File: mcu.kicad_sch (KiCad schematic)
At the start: 0 parts

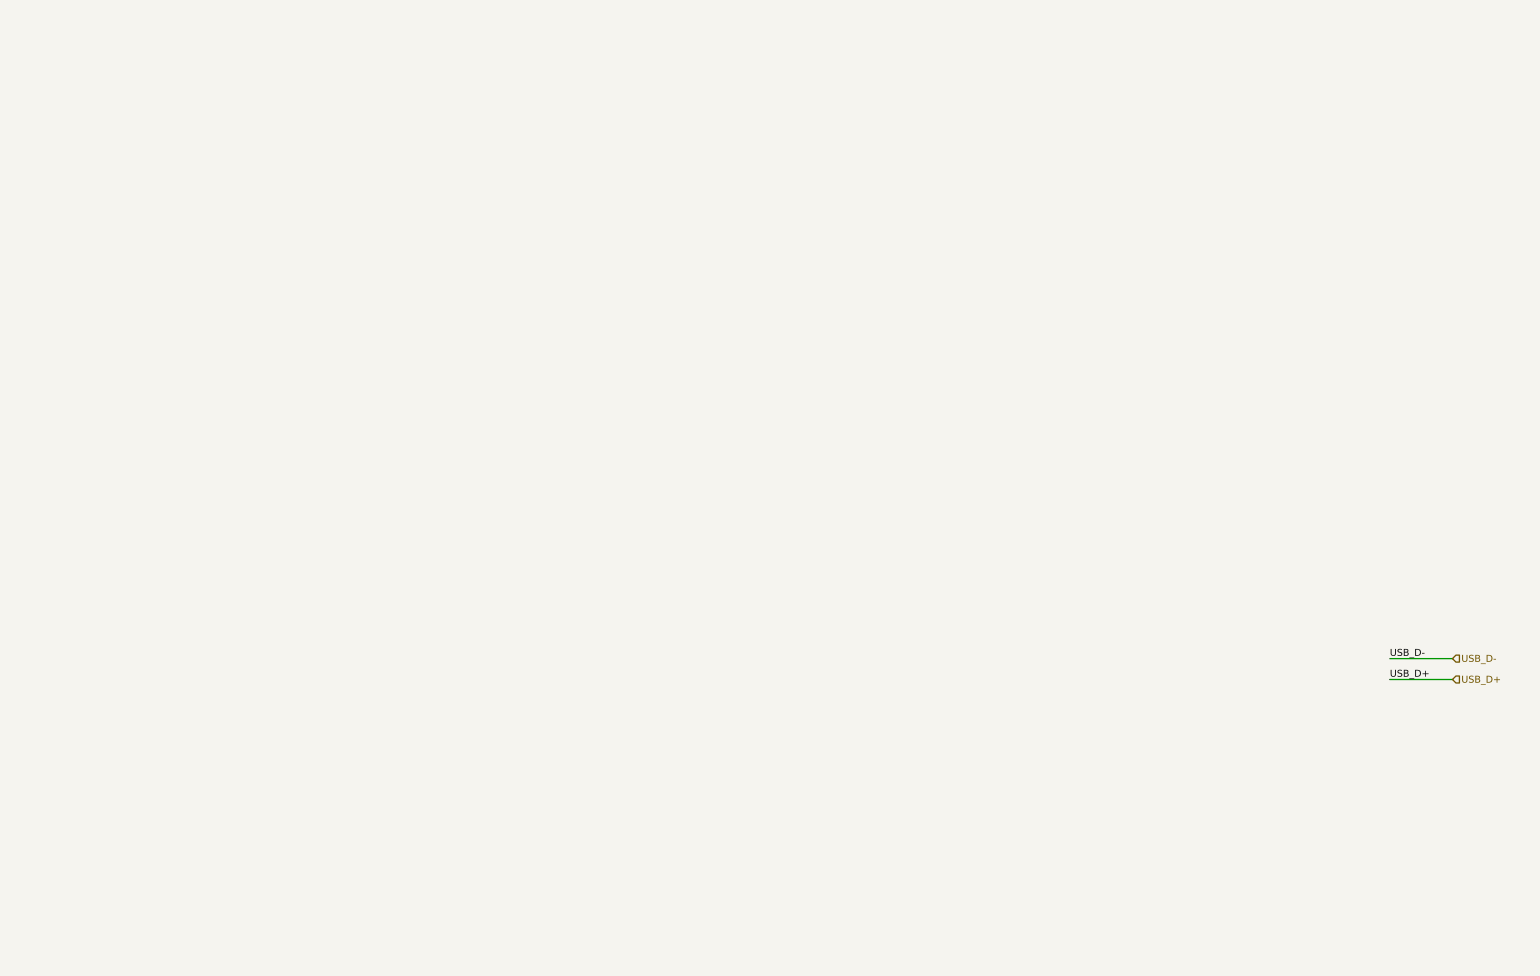
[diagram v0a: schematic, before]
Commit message: Add ESP32-S3-WROOM-1, 5V rail and UI sheet
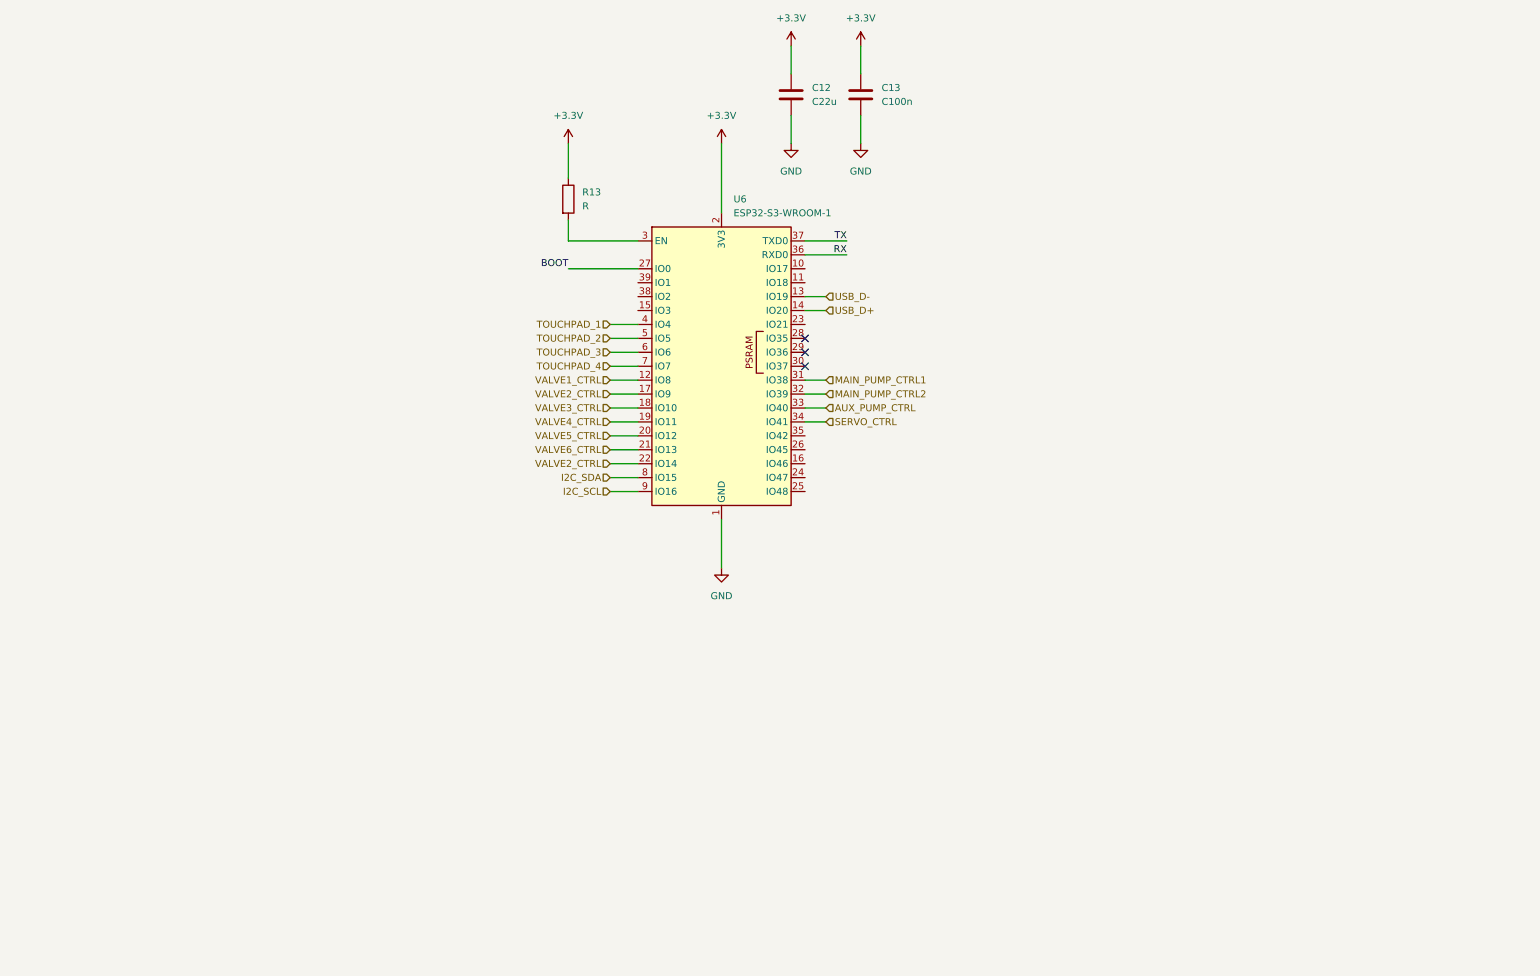
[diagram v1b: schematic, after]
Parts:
- added C12: C22u, symbol Device:C
- added C13: C100n, symbol Device:C
- added R13: R, symbol Device:R
- added U6: ESP32-S3-WROOM-1, RF_Module:ESP32-S3-WROOM-1, symbol RF_Module:ESP32-S3-WROOM-1
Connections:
- net USB_D+: now also U6.14 (IO20)
- net USB_D-: now also U6.13 (IO19)
- new net: R13.2, U6.3 (EN)
- new net +3.3V: C12.1, C13.1, R13.1, U6.2 (3V3)
- new net AUX_PUMP_CTRL: U6.33 (IO40)
- new net BOOT: U6.27 (IO0)
- new net GND: C12.2, C13.2, U6.1 (GND), U6.40 (GND), U6.41 (GND)
- new net I2C_SCL: U6.9 (IO16)
- new net I2C_SDA: U6.8 (IO15)
- new net MAIN_PUMP_CTRL1: U6.31 (IO38)
- new net MAIN_PUMP_CTRL2: U6.32 (IO39)
- new net RX: U6.36 (RXD0)
- new net SERVO_CTRL: U6.34 (IO41)
- new net TOUCHPAD_1: U6.4 (IO4)
- new net TOUCHPAD_2: U6.5 (IO5)
- new net TOUCHPAD_3: U6.6 (IO6)
- new net TOUCHPAD_4: U6.7 (IO7)
- new net TX: U6.37 (TXD0)
- new net VALVE1_CTRL: U6.12 (IO8)
- new net VALVE2_CTRL: U6.17 (IO9), U6.22 (IO14)
- new net VALVE3_CTRL: U6.18 (IO10)
- new net VALVE4_CTRL: U6.19 (IO11)
- new net VALVE5_CTRL: U6.20 (IO12)
- new net VALVE6_CTRL: U6.21 (IO13)
- no-connect marks 0 -> 3

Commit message: Finish first design
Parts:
- added C14: C22u, Capacitor_SMD:C_0805_2012Metric, symbol Device:C
- added JP2: SolderJumper_2_Bridged, Jumper:SolderJumper-2_P1.3mm_Bridged_RoundedPad1.0x1.5mm, symbol Jumper:SolderJumper_2_Bridged
- added R12, R15, R38: R4k7, Resistor_SMD:R_0805_2012Metric, symbol Device:R
- added TP10, TP11, TP12, TP13, TP14, TP16, TP17, TP5, TP6, TP7, TP8, TP9: TestPoint_Small, TestPoint:TestPoint_Pad_D1.5mm, symbol Connector:TestPoint_Small
- added U7: Pico, RPi_Pico:RPi_Pico_SMD_TH, symbol project:Pico
- C12: footprint (none) -> Capacitor_SMD:C_0805_2012Metric; Mouser Part Number (none) -> 187-CL21A226MQQNNNF
- C13: footprint (none) -> Capacitor_SMD:C_0603_1608Metric; Mouser Part Number (none) -> 80-C0603C104K3R7867
- R13: value R -> R100k; footprint (none) -> Resistor_SMD:R_0805_2012Metric; Mouser Part Number (none) -> 660-RK73B2ATTD104J
- U6: Mouser Part Number (none) -> 356-ESP32-S3WROOM1N4
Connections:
- net I2C_SDA is gone; now on net MAIN_PUMP_CTRL2: U6.8 (IO15)
- net TOUCHPAD_2 is gone; now on net AUX_PUMP_CTRL: U6.5 (IO5)
- net TOUCHPAD_4 is gone; now on net MAIN_PUMP_CTRL1: U6.7 (IO7)
- net +3.3V: now also C14.1, R12.1, R15.1, R38.1
- net AUX_PUMP_CTRL: no longer U6.33 (IO40)
- net BOOT: now also TP6.1
- net GND: now also C14.2, U7.43 (GND)
- net MAIN_PUMP_CTRL1: no longer U6.31 (IO38)
- net MAIN_PUMP_CTRL2: no longer U6.32 (IO39)
- net RX: now also TP16.1
- net SERVO_CTRL: now also U6.33 (IO40), TP10.1; no longer U6.34 (IO41)
- net TX: now also TP17.1
- net USB_D+: now also U7.41 (USB_D+)
- net USB_D-: now also U7.42 (USB_D-)
- net VALVE1_CTRL: now also U6.21 (IO13); no longer U6.12 (IO8)
- net VALVE2_CTRL: now also U6.20 (IO12); no longer U6.17 (IO9), U6.22 (IO14)
- net VALVE3_CTRL: now also U6.19 (IO11); no longer U6.18 (IO10)
- net VALVE4_CTRL: now also U6.18 (IO10); no longer U6.19 (IO11)
- net VALVE5_CTRL: now also U6.17 (IO9); no longer U6.20 (IO12)
- net VALVE6_CTRL: now also U6.16 (IO46); no longer U6.21 (IO13)
- net VALVE7_CTRL: now reaches U6.15 (IO3)
- net OLED_SDA: now reaches U6.23 (IO21)
- net OLED_SDA: now also R12.2, TP8.1
- net BUTTON_3: now reaches U6.26 (IO45)
- net ESP32_ENABLE: now reaches R13.2, U6.3 (EN)
- net ESP32_ENABLE: now also TP5.1
- net HX711_CLK: now reaches U6.35 (IO42)
- net HX711_CLK: now also TP11.1
- net BUZZER: now reaches U6.38 (IO2)
- net BUZZER: now also TP13.1
- net 1WIRE_TEMP: now reaches U6.39 (IO1)
- net 1WIRE_TEMP: now also R38.2, TP14.1
- net I2C_SCL: no longer names the net of U6.9 (IO16)
- net TOUCHPAD_1 renamed PWR_FAULT
- net PWR_FAULT: now also TP9.1
- net TOUCHPAD_3 renamed WATER_LEVEL_SENSOR_PIN
- net WATER_LEVEL_SENSOR_PIN: now also JP2.1 (A)
- new net: U7.13 (GND), U7.18 (GND), U7.3 (GND), U7.8 (GND)
- new net: U7.23 (GND), U7.28 (GND), U7.38 (GND)
- new net BUTTON_1: U6.32 (IO39)
- new net BUTTON_2: U6.31 (IO38)
- new net HX711_DAT: TP12.1, U6.34 (IO41)
- new net OLED_SCL: R15.2, TP7.1, U6.22 (IO14)
- new net WATER_LEVEL_SENSOR: JP2.2 (B)
- no-connect marks 3 -> 10
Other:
- note added: "<- Alternatives ->"
- note added: "Check: TODO (boot pin states, alternate funcs)"
- note added: "Don't use PSRAM pins"
- note added: "Don't use pins"
- note added: "ESP32-S3"
- note added: "I2C Pull-Ups"
- note added: "Module cost for ESP32-S3-WROOM-1-XXX: ~3-4 Euro"
- note added: "Module cost for Pico / Pico W: 4~7 Euro"
- note added: "RPI-PICO-W"
- title: (none) -> openautolab - Mainboard
- moved on the sheet: C12, C13, R13, U6

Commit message: Add screen FPC to schematic and remove old OLED stuff
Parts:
- removed C14: C22u, Capacitor_SMD:C_0805_2012Metric, symbol Device:C
- removed JP2: SolderJumper_2_Bridged, Jumper:SolderJumper-2_P1.3mm_Bridged_RoundedPad1.0x1.5mm, symbol Jumper:SolderJumper_2_Bridged
- removed U7: Pico, RPi_Pico:RPi_Pico_SMD_TH, symbol project:Pico
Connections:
- net BUTTON_1: no longer names the net of U6.32 (IO39)
- net BUTTON_2: no longer names the net of U6.31 (IO38)
- net BUTTON_3: no longer names the net of U6.26 (IO45)
- net OLED_SCL: no longer names the net of TP7.1, U6.22 (IO14)
- net OLED_SCL: no longer R15.2
- net OLED_SDA: no longer names the net of TP8.1, U6.23 (IO21)
- net OLED_SDA: no longer R12.2
- net WATER_LEVEL_SENSOR_PIN renamed FLOW_SENSOR
- new net LCD_TOUCH_SCL: R15.2
- new net LCD_TOUCH_SDA: R12.2
- no-connect marks 10 -> 5
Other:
- note removed: "Module cost for Pico / Pico W: 4~7 Euro"
- note removed: "RPI-PICO-W"

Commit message: Fix LCD connector pin mapping and map them to MCU pins
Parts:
- added TP1, TP15, TP2, TP23, TP24, TP27, TP3, TP4: TestPoint_Small, TestPoint:TestPoint_Pad_D1.5mm, symbol Connector:TestPoint_Small
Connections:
- net FLOW_SENSOR: now also TP2.1
- net LCD_MISO: now also U6.11 (IO18), TP15.1
- net LCD_MOSI: now also U6.10 (IO17), TP4.1
- net LCD_RESET: now also U6.9 (IO16), TP1.1
- net LCD_RS: now also U6.12 (IO8), TP3.1
- net LCD_SCK: now also TP7.1, U6.22 (IO14)
- net LCD_TOUCH_INT: now also U6.26 (IO45), TP23.1
- net LCD_TOUCH_RESET: now also TP8.1, U6.23 (IO21)
- net LCD_TOUCH_SCL: now also U6.32 (IO39), TP24.1
- net LCD_TOUCH_SDA: now also U6.31 (IO38), TP27.1

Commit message: Finalize pin mapping, cleanup and layout
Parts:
- removed TP1, TP10, TP11, TP12, TP13, TP14, TP15, TP2, TP23, TP24, TP27, TP3, TP4, TP7, TP8, TP9: TestPoint_Small, TestPoint:TestPoint_Pad_D1.5mm, symbol Connector:TestPoint_Small
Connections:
- net 1WIRE_TEMP: now also U6.9 (IO16); no longer U6.39 (IO1)
- net AUX_PUMP_CTRL: now also U6.12 (IO8); no longer U6.5 (IO5)
- net BUZZER: now also U6.5 (IO5); no longer U6.38 (IO2)
- net FLOW_SENSOR: now also U6.8 (IO15); no longer U6.6 (IO6)
- net HX711_CLK: now also U6.6 (IO6); no longer U6.35 (IO42)
- net HX711_DAT: now also U6.7 (IO7); no longer U6.34 (IO41)
- net LCD_MISO: now also U6.33 (IO40); no longer U6.11 (IO18)
- net LCD_MOSI: now also U6.31 (IO38); no longer U6.10 (IO17)
- net LCD_RESET: now also U6.23 (IO21); no longer U6.9 (IO16)
- net LCD_RS: now also U6.26 (IO45); no longer U6.12 (IO8)
- net LCD_SCK: now also U6.32 (IO39); no longer U6.22 (IO14)
- net LCD_TOUCH_INT: now also U6.34 (IO41); no longer U6.26 (IO45)
- net LCD_TOUCH_RESET: now also U6.35 (IO42); no longer U6.23 (IO21)
- net LCD_TOUCH_SCL: now also U6.22 (IO14); no longer U6.32 (IO39)
- net LCD_TOUCH_SDA: now also U6.38 (IO2); no longer U6.31 (IO38)
- net MAIN_PUMP_CTRL1: now also U6.11 (IO18); no longer U6.7 (IO7)
- net MAIN_PUMP_CTRL2: now also U6.10 (IO17); no longer U6.8 (IO15)
- net SERVO_CTRL: now also U6.39 (IO1); no longer U6.33 (IO40)

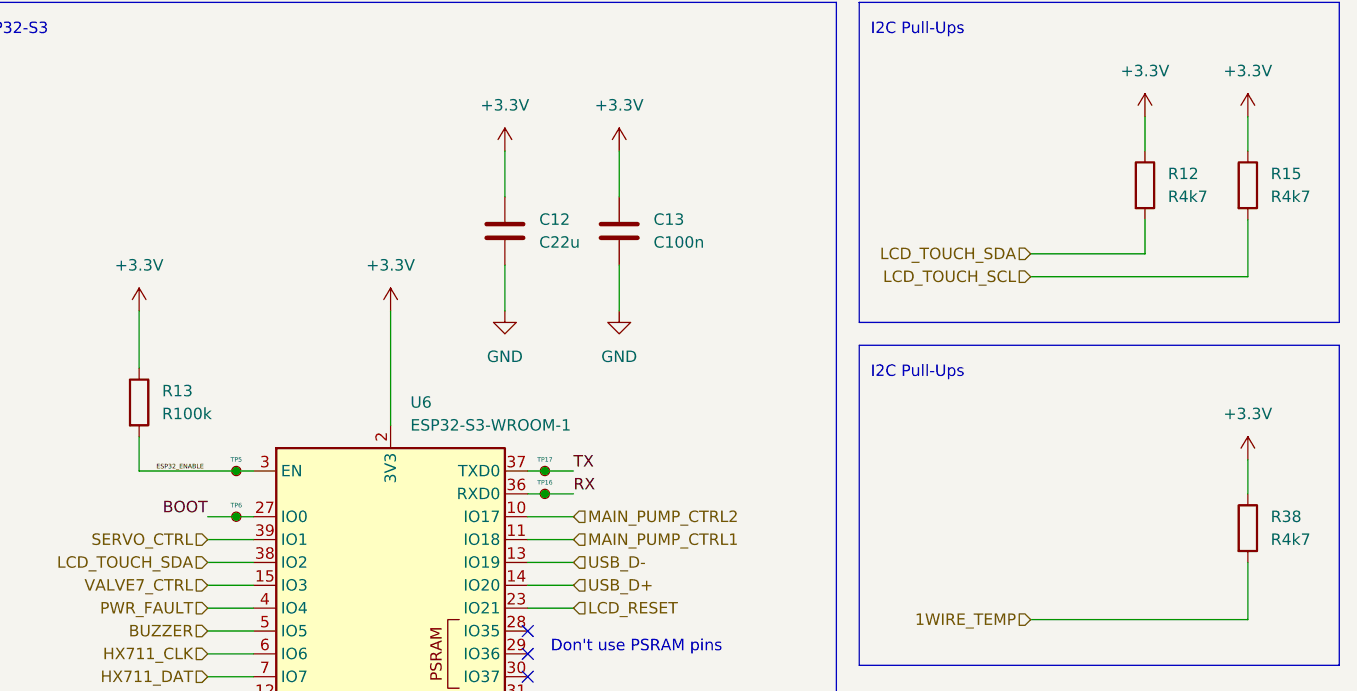
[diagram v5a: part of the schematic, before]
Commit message: Re-annotate parts by board
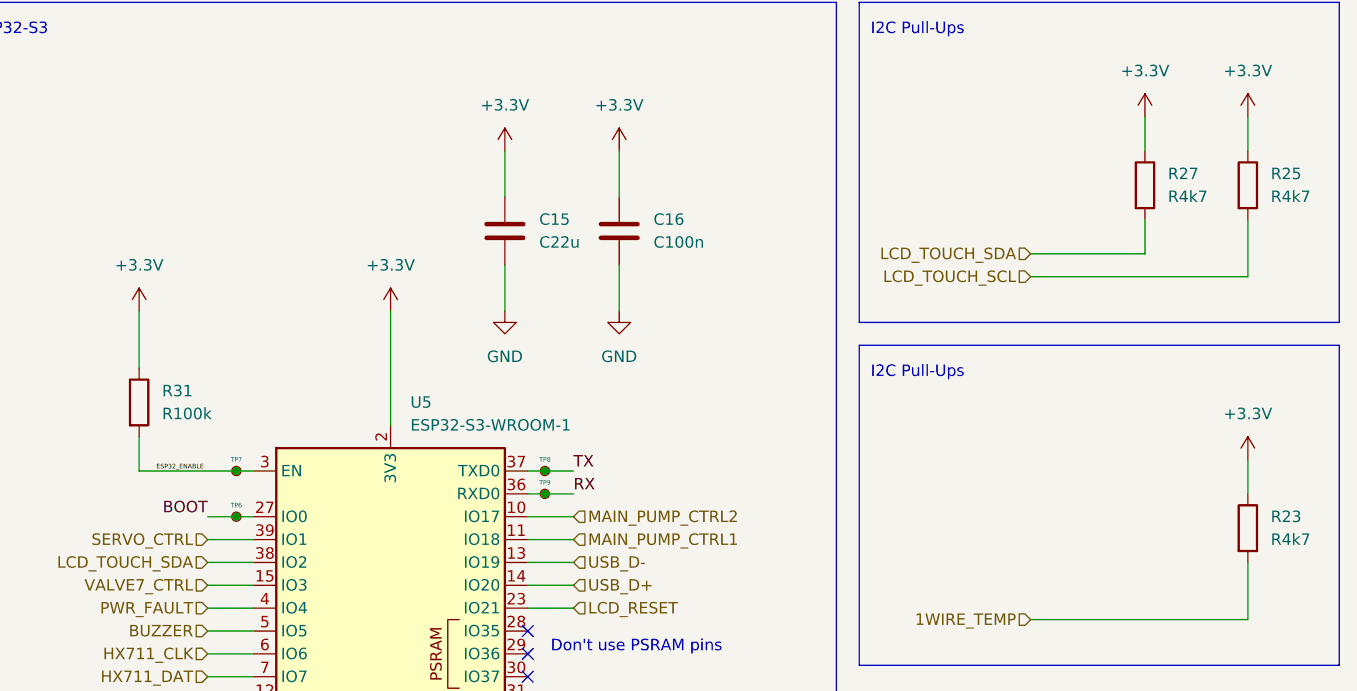
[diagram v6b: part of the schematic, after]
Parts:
- renumbered C12 to C15, C13 to C16, R38 to R23, R15 to R25, R12 to R27, R13 to R31, TP5 to TP7, TP17 to TP8, TP16 to TP9, U6 to U5
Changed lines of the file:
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@@
   (symbol (lib_id "Connector:TestPoint_Small") (at 46.355 82.55 0) (unit 1)
     (in_bom yes) (on_board yes) (dnp no)
-    (property "Reference" "TP5" (at 46.355 81.28 0)
+    (property "Reference" "TP7" (at 46.355 81.28 0)
       (effects (font (size 0.504 0.504)))
     )
@@
       (project "mainboard"
         (path "/613f8c39-c37c-4981-8911-5138d36a7959/ed2e236e-cfd2-4567-8f0f-a7cfa7de4717"
-          (reference "TP5") (unit 1)
+          (reference "TP7") (unit 1)
         )
       )
@@
   (symbol (lib_id "Connector:TestPoint_Small") (at 80.645 82.55 0) (unit 1)
     (in_bom yes) (on_board yes) (dnp no)
-    (property "Reference" "TP17" (at 80.645 81.28 0)
+    (property "Reference" "TP8" (at 80.645 81.28 0)
       (effects (font (size 0.504 0.504)))
     )
@@
       (project "mainboard"
         (path "/613f8c39-c37c-4981-8911-5138d36a7959/ed2e236e-cfd2-4567-8f0f-a7cfa7de4717"
-          (reference "TP17") (unit 1)
+          (reference "TP8") (unit 1)
         )
       )
@@
   (symbol (lib_id "Device:C") (at 76.2 55.88 0) (unit 1)
     (in_bom yes) (on_board yes) (dnp no) (fields_autoplaced)
-    (property "Reference" "C12" (at 80.01 54.61 0)
+    (property "Reference" "C15" (at 80.01 54.61 0)
       (effects (font (size 1.27 1.27)) (justify left))
     )
@@
       (project "mainboard"
         (path "/613f8c39-c37c-4981-8911-5138d36a7959/ed2e236e-cfd2-4567-8f0f-a7cfa7de4717"
-          (reference "C12") (unit 1)
+          (reference "C15") (unit 1)
         )
       )
@@
   (symbol (lib_id "Connector:TestPoint_Small") (at 80.645 85.09 0) (unit 1)
     (in_bom yes) (on_board yes) (dnp no)
-    (property "Reference" "TP16" (at 80.645 83.82 0)
+    (property "Reference" "TP9" (at 80.645 83.82 0)
       (effects (font (size 0.504 0.504)))
     )
@@
       (project "mainboard"
         (path "/613f8c39-c37c-4981-8911-5138d36a7959/ed2e236e-cfd2-4567-8f0f-a7cfa7de4717"
-          (reference "TP16") (unit 1)
+          (reference "TP9") (unit 1)
         )
       )
@@
   (symbol (lib_id "Device:R") (at 158.75 50.8 0) (unit 1)
     (in_bom yes) (on_board yes) (dnp no) (fields_autoplaced)
-    (property "Reference" "R15" (at 161.29 49.53 0)
+    (property "Reference" "R25" (at 161.29 49.53 0)
       (effects (font (size 1.27 1.27)) (justify left))
     )
@@
       (project "mainboard"
         (path "/613f8c39-c37c-4981-8911-5138d36a7959/ed2e236e-cfd2-4567-8f0f-a7cfa7de4717"
-          (reference "R15") (unit 1)
+          (reference "R25") (unit 1)
         )
       )
@@
   (symbol (lib_id "RF_Module:ESP32-S3-WROOM-1") (at 63.5 105.41 0) (unit 1)
     (in_bom yes) (on_board yes) (dnp no) (fields_autoplaced)
-    (property "Reference" "U6" (at 65.6941 74.93 0)
+    (property "Reference" "U5" (at 65.6941 74.93 0)
       (effects (font (size 1.27 1.27)) (justify left))
     )
@@
       (project "mainboard"
         (path "/613f8c39-c37c-4981-8911-5138d36a7959/ed2e236e-cfd2-4567-8f0f-a7cfa7de4717"
-          (reference "U6") (unit 1)
+          (reference "U5") (unit 1)
         )
       )
@@
   (symbol (lib_id "Device:R") (at 147.32 50.8 0) (unit 1)
     (in_bom yes) (on_board yes) (dnp no) (fields_autoplaced)
-    (property "Reference" "R12" (at 149.86 49.53 0)
+    (property "Reference" "R27" (at 149.86 49.53 0)
       (effects (font (size 1.27 1.27)) (justify left))
     )
@@
       (project "mainboard"
         (path "/613f8c39-c37c-4981-8911-5138d36a7959/ed2e236e-cfd2-4567-8f0f-a7cfa7de4717"
-          (reference "R12") (unit 1)
+          (reference "R27") (unit 1)
         )
       )
@@
   (symbol (lib_id "Device:R") (at 35.56 74.93 0) (unit 1)
     (in_bom yes) (on_board yes) (dnp no) (fields_autoplaced)
-    (property "Reference" "R13" (at 38.1 73.66 0)
+    (property "Reference" "R31" (at 38.1 73.66 0)
       (effects (font (size 1.27 1.27)) (justify left))
     )
@@
       (project "mainboard"
         (path "/613f8c39-c37c-4981-8911-5138d36a7959/ed2e236e-cfd2-4567-8f0f-a7cfa7de4717"
-          (reference "R13") (unit 1)
+          (reference "R31") (unit 1)
         )
       )
@@
   (symbol (lib_id "Device:R") (at 158.75 88.9 0) (unit 1)
     (in_bom yes) (on_board yes) (dnp no) (fields_autoplaced)
-    (property "Reference" "R38" (at 161.29 87.63 0)
+    (property "Reference" "R23" (at 161.29 87.63 0)
       (effects (font (size 1.27 1.27)) (justify left))
     )
@@
       (project "mainboard"
         (path "/613f8c39-c37c-4981-8911-5138d36a7959/ed2e236e-cfd2-4567-8f0f-a7cfa7de4717"
-          (reference "R38") (unit 1)
+          (reference "R23") (unit 1)
         )
       )
@@
   (symbol (lib_id "Device:C") (at 88.9 55.88 0) (unit 1)
     (in_bom yes) (on_board yes) (dnp no) (fields_autoplaced)
-    (property "Reference" "C13" (at 92.71 54.61 0)
+    (property "Reference" "C16" (at 92.71 54.61 0)
       (effects (font (size 1.27 1.27)) (justify left))
     )
@@
       (project "mainboard"
         (path "/613f8c39-c37c-4981-8911-5138d36a7959/ed2e236e-cfd2-4567-8f0f-a7cfa7de4717"
-          (reference "C13") (unit 1)
-        )
-      )
+          (reference "C16") (unit 1)
+        )
+      )
